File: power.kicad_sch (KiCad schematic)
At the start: 15 parts, among them U4 AP64501

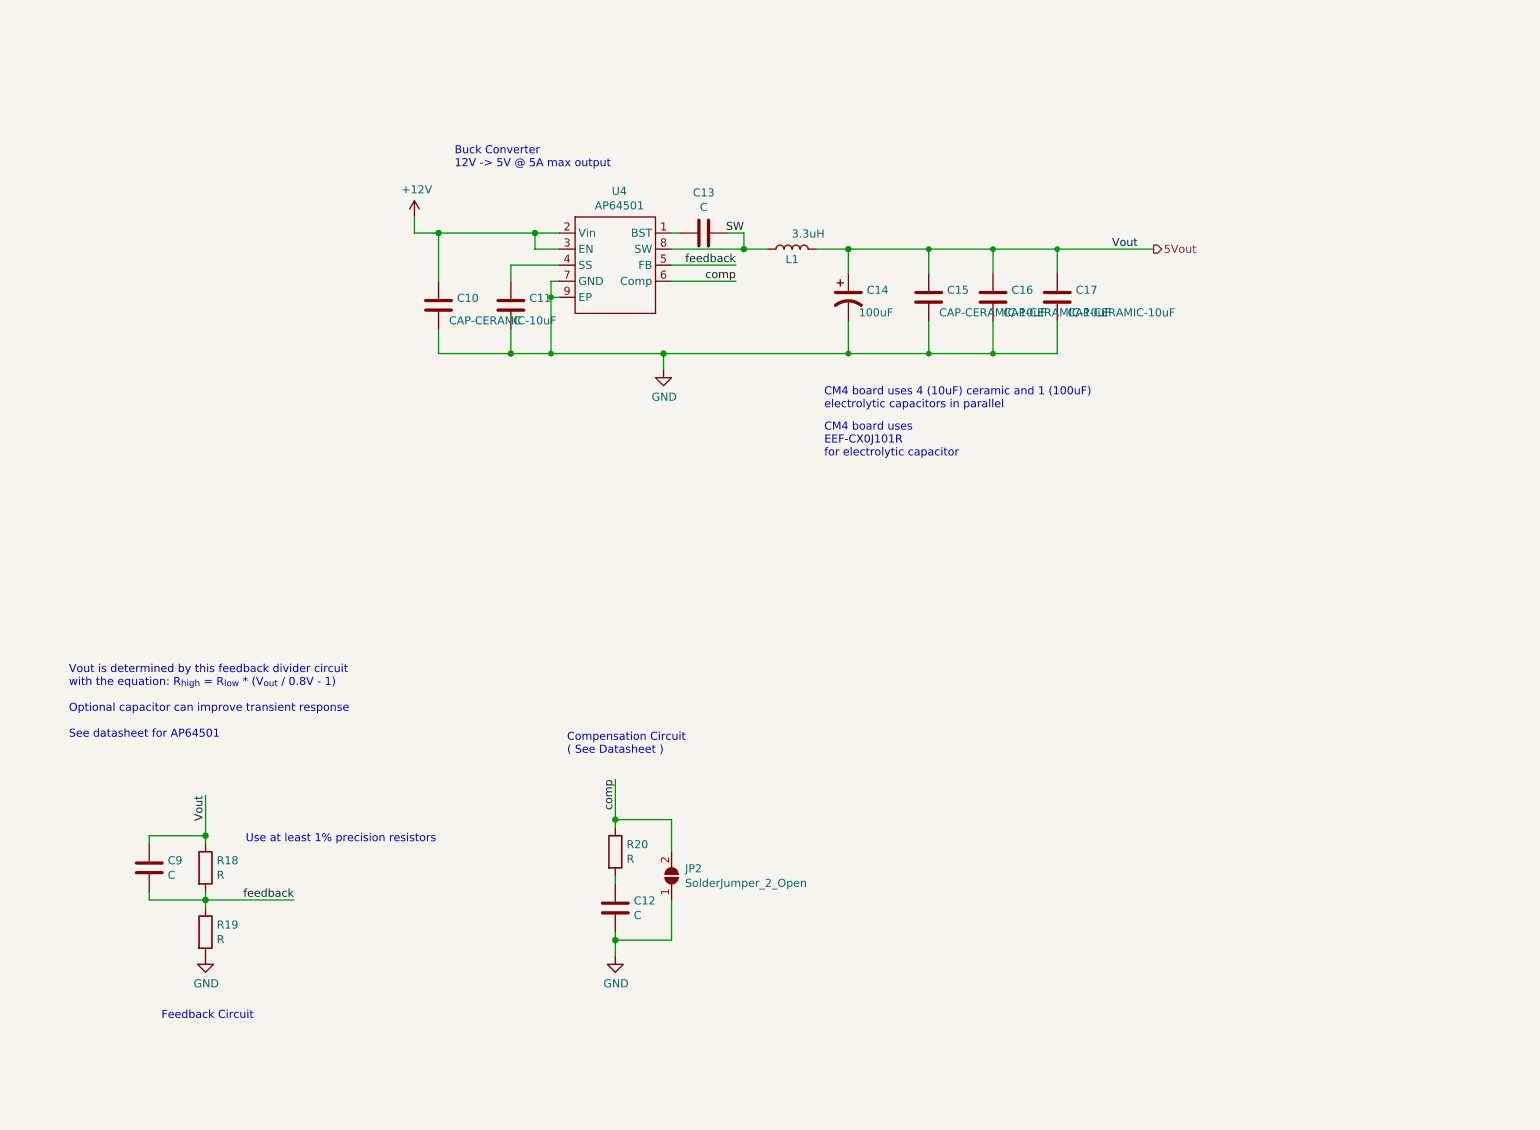
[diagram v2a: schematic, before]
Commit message: Cleaning up
Reassigned reference designators to better match their position on the board.
Moved USB hub IC and related circuits to their own sheet in the schematic.
Tweaked reference designator positions on board to improve visibility.
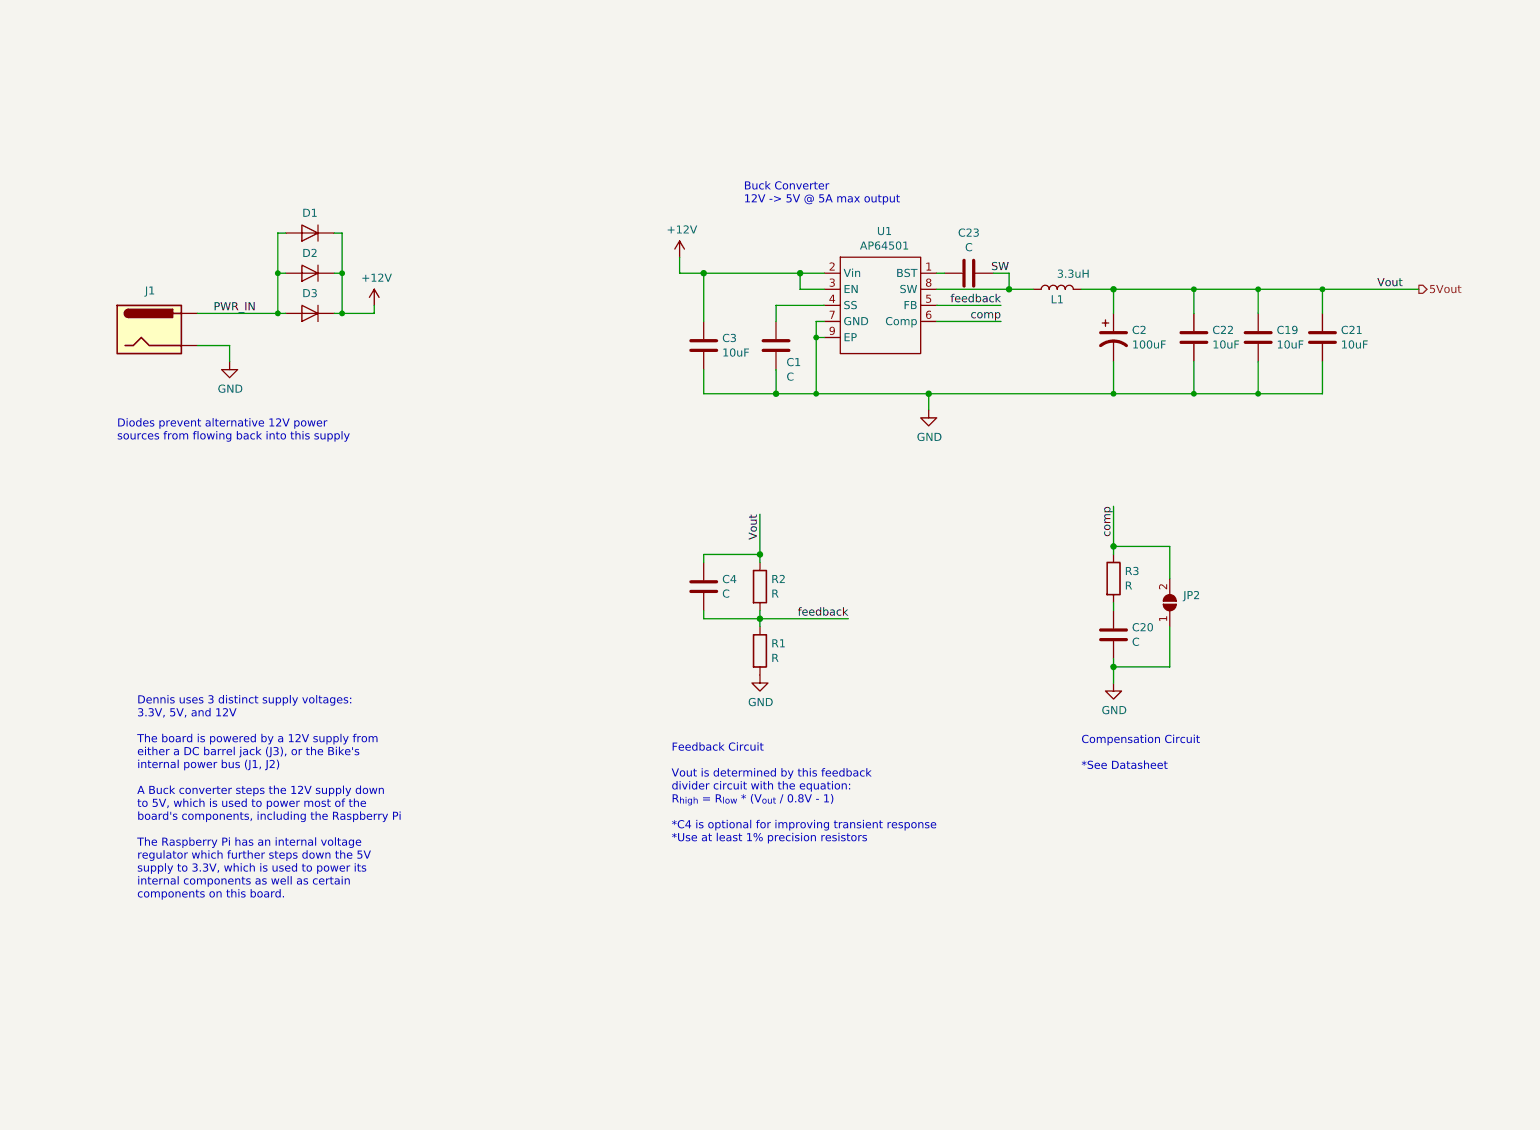
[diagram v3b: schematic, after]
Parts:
- added D1, D2, D3: Diode, Diode_SMD:D_SOD-123F, symbol symbols:Diode
- added J1: Barrel_Jack, Connector_BarrelJack:BarrelJack_Horizontal, symbol symbols:Barrel_Jack
- C19: renamed from C16; value CAP-CERAMIC-10uF -> 10uF
- C21: renamed from C17; value CAP-CERAMIC-10uF -> 10uF
- C22: renamed from C15; value CAP-CERAMIC-10uF -> 10uF
- C3: renamed from C10; value CAP-CERAMIC-10uF -> 10uF
- renumbered C11 to C1, C14 to C2, C12 to C20, C13 to C23, C9 to C4, R19 to R1, R18 to R2, R20 to R3, U4 to U1
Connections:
- net +12V: now also D1.1 (K), D2.1 (K), D3.1 (K)
- net GND: now also J1.2
- new net PWR_IN: D1.2 (A), D2.2 (A), D3.2 (A), J1.1
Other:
- note added: "Compensation Circuit *See Datasheet"
- note added: "Dennis uses 3 distinct supply voltages: 3.3V, 5V, and 12V The board is powered by a 12V supply from either a DC barrel jack (J3), or the Bike's internal power bus (J1, J2) A Buck converter steps the 12V supply down to 5V, which is used to power most of the board's components, including the Raspberry Pi The Raspberry Pi has an internal voltage regulator which further steps down the 5V supply to 3.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"
- note added: "Diodes prevent alternative 12V power sources from flowing back into this supply"
- note added: "Feedback Circuit Vout is determined by this feedback divider circuit with the equation: R_{high} = R_{low} * (V_{out} / 0.8V - 1) *C4 is optional for improving transient response *Use at least 1% precision resistors"
- note removed: "CM4 board uses 4 (10uF) ceramic and 1 (100uF) electrolytic capacitors in parallel"
- note removed: "CM4 board uses EEF-CX0J101R for electrolytic capacitor"
- note removed: "Compensation Circuit ( See Datasheet )"
- note removed: "Feedback Circuit"
- note removed: "Use at least 1% precision resistors"
- note removed: "Vout is determined by this feedback divider circuit with the equation: R_{high} = R_{low} * (V_{out} / 0.8V - 1) Optional capacitor can improve transient response See datasheet for AP64501"
- moved on the sheet: C1, C19, C2, C20, C21, C22, C23, C3, C4, JP2, L1, R1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

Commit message: layout sketching
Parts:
- added C10, C11, C9: C, Capacitor_SMD:C_0805_2012Metric, symbol Device:C
- added U9: TPS79933, Package_TO_SOT_SMD:SOT-23-5, symbol flip-pixel:TPS79933
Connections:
- net GND: now also C10.2, C11.2, C9.2, U9.2 (GND)
- new net: C9.1, U9.4 (NR)
- new net +3V3: C11.1, U9.5 (OUT)
- new net +5V: C10.1, U9.1 (IN)
- new net enable: U9.3 (EN)
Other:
- note added: "Near U? (Input)"
- note added: "Near U? (Output)"
- moved on the sheet: C1, C19, C2, C20, C21, C22, C23, C3, C4, D1, D2, D3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

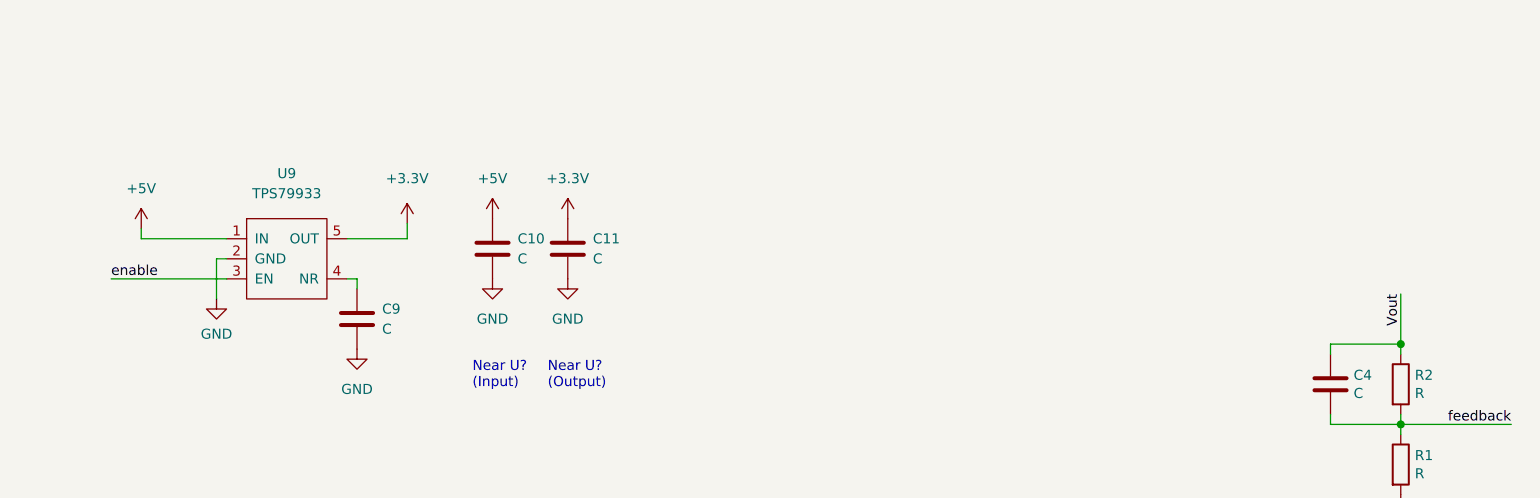
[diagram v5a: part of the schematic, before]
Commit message: components group and placed in roughly the right position
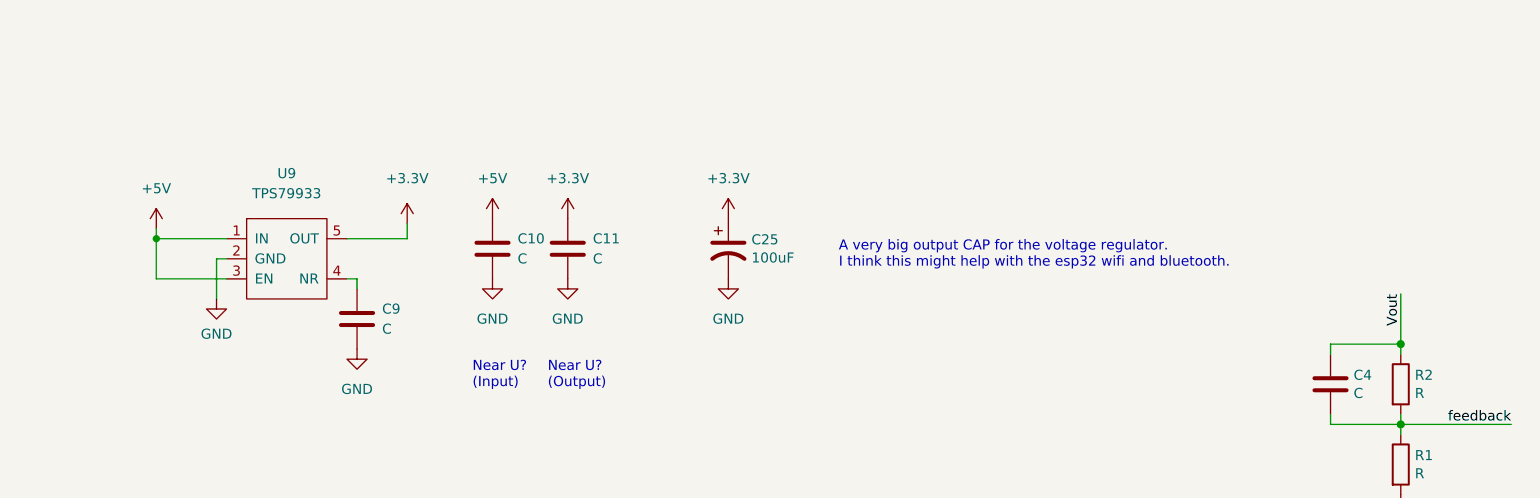
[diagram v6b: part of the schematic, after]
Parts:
- added C25: 100uF, Capacitor_SMD:CP_Elec_6.3x5.9, symbol symbols:100uF
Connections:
- net enable is gone; now on net +5V: U9.3 (EN)
- net +3V3: now also C25.1
- net GND: now also C25.2
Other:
- note added: "A very big output CAP for the voltage regulator. I think this might help with the esp32 wifi and bluetooth."
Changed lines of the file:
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@@
     (company "eCafe Racer")
   )
+  (junction (at 36.83 106.68) (diameter 0.9144) (color 0 0 0 0))
   (junction (at 57.15 36.83) (diameter 0.9144) (color 0 0 0 0))
   (junction (at 57.15 43.18) (diameter 0.9144) (color 0 0 0 0))
@@
   (junction (at 238.125 122.555) (diameter 1.016) (color 0 0 0 0))
   (junction (at 238.125 141.605) (diameter 1.016) (color 0 0 0 0))
-  (wire (pts (xy 31.115 111.76) (xy 45.72 111.76))
-    (stroke (width 0) (type solid) (color 0 0 0 0))
-  )
-  (wire (pts (xy 34.925 105.41) (xy 34.925 106.68))
+  (wire (pts (xy 36.83 105.41) (xy 36.83 106.68))
+    (stroke (width 0) (type solid) (color 0 0 0 0))
+  )
+  (wire (pts (xy 36.83 111.76) (xy 36.83 106.68))
     (stroke (width 0) (type solid) (color 0 0 0 0))
   )
@@
     (stroke (width 0) (type solid) (color 0 0 0 0))
   )
-  (wire (pts (xy 45.72 106.68) (xy 34.925 106.68))
+  (wire (pts (xy 45.72 106.68) (xy 36.83 106.68))
     (stroke (width 0) (type solid) (color 0 0 0 0))
   )
   (wire (pts (xy 45.72 109.22) (xy 44.45 109.22))
+    (stroke (width 0) (type solid) (color 0 0 0 0))
+  )
+  (wire (pts (xy 45.72 111.76) (xy 36.83 111.76))
     (stroke (width 0) (type solid) (color 0 0 0 0))
   )
@@
     (effects (font (size 1.27 1.27)) (justify left bottom))
   )
+  (text "A very big output CAP for the voltage regulator.\nI think this might help with the esp32 wifi and bluetooth."
+    (at 123.19 110.49 0)
+    (effects (font (size 1.27 1.27)) (justify left bottom))
+  )
   (text "Feedback Circuit\n\nVout is determined by this feedback\ndivider circuit with the equation:\nR_{high} = R_{low} * (V_{out} / 0.8V - 1)\n\n*C4 is optional for improving transient response\n*Use at least 1% precision resistors"
     (at 180.34 165.735 0)
@@
     (effects (font (size 1.27 1.27)) (justify left bottom))
   )
-  (label "enable" (at 31.115 111.76 0)
-    (effects (font (size 1.27 1.27)) (justify left bottom))
-  )
   (label "PWR_IN" (at 46.99 43.18 0)
     (effects (font (size 1.27 1.27)) (justify left bottom))
@@
     (effects (font (size 1.27 1.27)) (justify left))
   )
-  (symbol (lib_id "power:+5V") (at 34.925 105.41 0) (unit 1)
-    (in_bom yes) (on_board yes) (fields_autoplaced)
-    (property "Reference" "#PWR0127" (id 0) (at 34.925 109.22 0)
-      (effects (font (size 1.27 1.27)) hide)
-    )
-    (property "Value" "+5V" (id 1) (at 34.925 100.33 0))
-    (property "Footprint" "" (id 2) (at 34.925 105.41 0)
-      (effects (font (size 1.27 1.27)) hide)
-    )
-    (property "Datasheet" "" (id 3) (at 34.925 105.41 0)
+  (symbol (lib_id "power:+5V") (at 36.83 105.41 0) (unit 1)
+    (in_bom yes) (on_board yes) (fields_autoplaced)
+    (property "Reference" "#PWR0127" (id 0) (at 36.83 109.22 0)
+      (effects (font (size 1.27 1.27)) hide)
+    )
+    (property "Value" "+5V" (id 1) (at 36.83 100.33 0))
+    (property "Footprint" "" (id 2) (at 36.83 105.41 0)
+      (effects (font (size 1.27 1.27)) hide)
+    )
+    (property "Datasheet" "" (id 3) (at 36.83 105.41 0)
       (effects (font (size 1.27 1.27)) hide)
     )
@@
     (pin "1")
   )
+  (symbol (lib_id "power:+3.3V") (at 109.22 104.14 0) (unit 1)
+    (in_bom yes) (on_board yes) (fields_autoplaced)
+    (property "Reference" "#PWR0142" (id 0) (at 109.22 107.95 0)
+      (effects (font (size 1.27 1.27)) hide)
+    )
+    (property "Value" "+3.3V" (id 1) (at 109.22 99.06 0))
+    (property "Footprint" "" (id 2) (at 109.22 104.14 0)
+      (effects (font (size 1.27 1.27)) hide)
+    )
+    (property "Datasheet" "" (id 3) (at 109.22 104.14 0)
+      (effects (font (size 1.27 1.27)) hide)
+    )
+    (pin "1")
+  )
   (symbol (lib_id "power:GND") (at 44.45 114.3 0) (unit 1)
     (in_bom yes) (on_board yes) (fields_autoplaced)
@@
     )
     (property "Datasheet" "" (id 3) (at 88.9 111.76 0)
+      (effects (font (size 1.27 1.27)) hide)
+    )
+    (pin "1")
+  )
+  (symbol (lib_id "power:GND") (at 109.22 111.76 0) (unit 1)
+    (in_bom yes) (on_board yes) (fields_autoplaced)
+    (property "Reference" "#PWR0143" (id 0) (at 109.22 118.11 0)
+      (effects (font (size 1.27 1.27)) hide)
+    )
+    (property "Value" "GND" (id 1) (at 109.22 116.84 0))
+    (property "Footprint" "" (id 2) (at 109.22 111.76 0)
+      (effects (font (size 1.27 1.27)) hide)
+    )
+    (property "Datasheet" "" (id 3) (at 109.22 111.76 0)
       (effects (font (size 1.27 1.27)) hide)
     )
@@
       (effects (font (size 1.27 1.27)) hide)
     )
+    (pin "1")
+    (pin "2")
+  )
+  (symbol (lib_id "symbols:100uF") (at 109.22 107.95 0) (unit 1)
+    (in_bom yes) (on_board yes)
+    (property "Reference" "C25" (id 0) (at 112.1411 106.8006 0)
+      (effects (font (size 1.27 1.27)) (justify left))
+    )
+    (property "Value" "100uF" (id 1) (at 112.1411 109.0993 0)
+      (effects (font (size 1.27 1.27)) (justify left))
+    )
+    (property "Footprint" "Capacitor_SMD:CP_Elec_6.3x5.9" (id 2) (at 109.22 107.95 0)
+      (effects (font (size 1.27 1.27)) hide)
+    )
+    (property "Datasheet" "https://content.kemet.com/datasheets/KEM_A4088_A768.pdf" (id 3) (at 109.22 107.95 0)
+      (effects (font (size 1.27 1.27)) hide)
+    )
+    (property "Vendor" "Digikey" (id 4) (at 109.22 107.95 0)
+      (effects (font (size 1.27 1.27)) hide)
+    )
+    (property "Vendor Part" "399-A768EB107M1ELAS036CT-ND" (id 5) (at 109.22 107.95 0)
+      (effects (font (size 1.27 1.27)) hide)
+    )
+    (property "Manufacuturer" "KEMET" (id 6) (at 109.22 107.95 0)
+      (effects (font (size 1.27 1.27)) hide)
+    )
+    (property "Manufacturer Part" "A768EB107M1ELAS036" (id 7) (at 109.22 107.95 0)
+      (effects (font (size 1.27 1.27)) hide)
+    )
+    (property "Voltage" "25V" (id 8) (at 109.22 107.95 0)
+      (effects (font (size 1.27 1.27)) hide)
+    )
